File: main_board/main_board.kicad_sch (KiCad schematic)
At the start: 32 parts, among them Q1 NMOS, U1 STM32G031G8Ux, U2 AMS1117-3.3

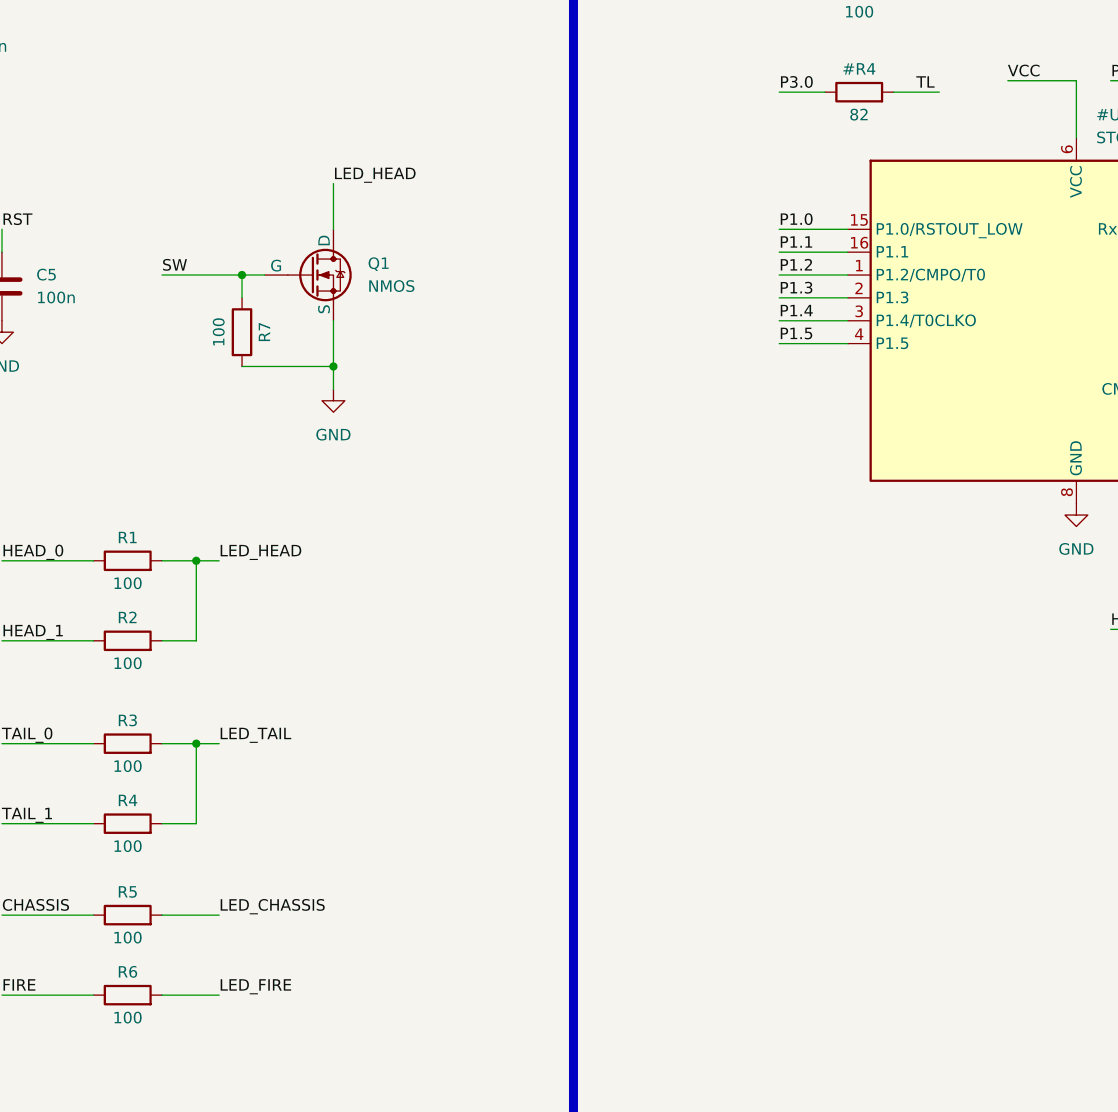
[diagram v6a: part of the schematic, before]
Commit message: feat(main_board): modify placement
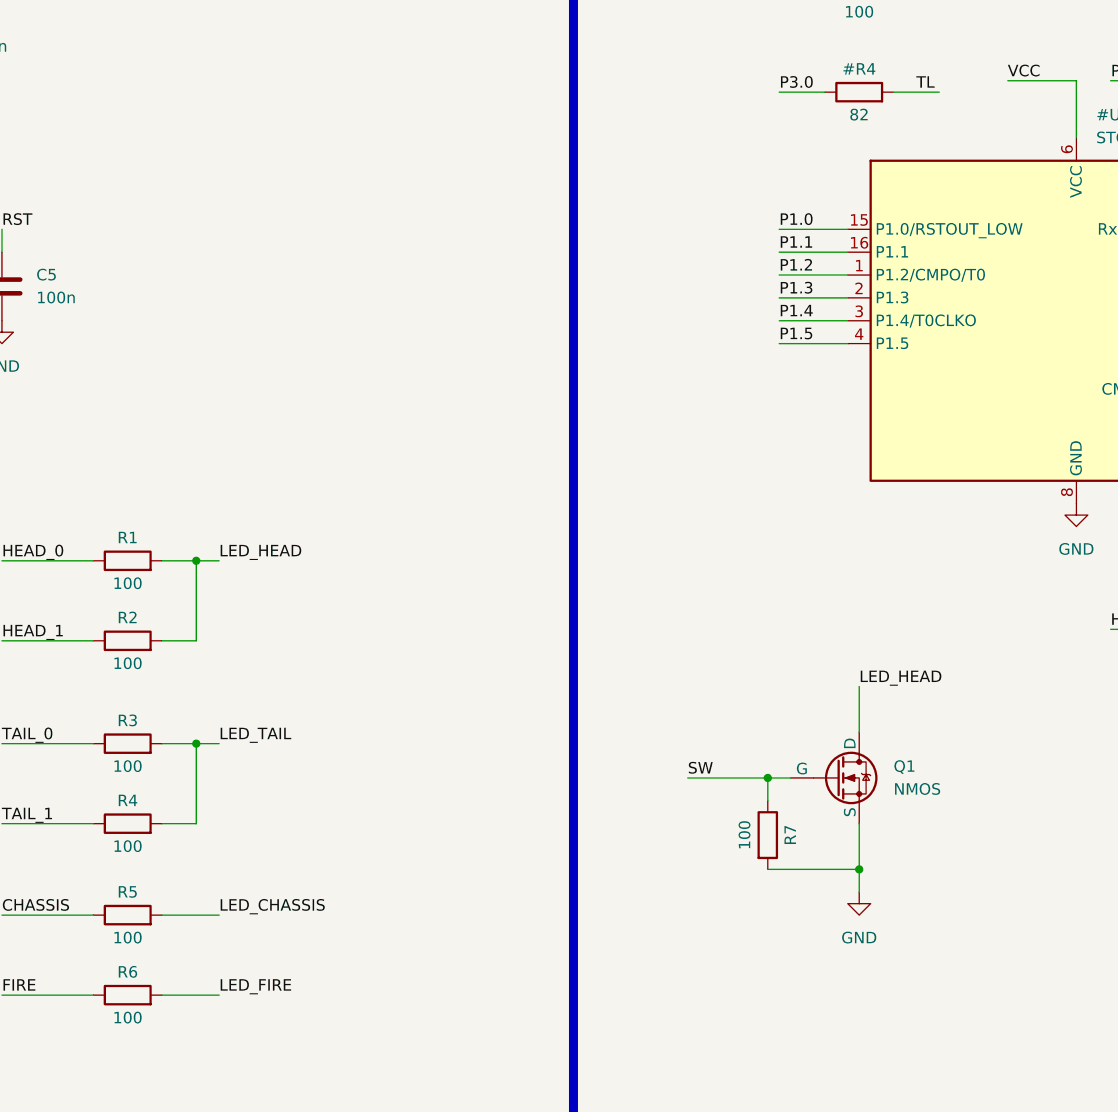
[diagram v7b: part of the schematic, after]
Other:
- moved on the sheet: Q1, R7
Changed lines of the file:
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@@
   (junction (at 119.38 140.97) (diameter 0) (color 0 0 0 0)
   )
-  (junction (at 134.62 99.06) (diameter 0) (color 0 0 0 0)
+  (junction (at 193.04 154.94) (diameter 0) (color 0 0 0 0)
   )
   (junction (at 50.8 58.42) (diameter 0) (color 0 0 0 0)
@@
   (junction (at 119.38 120.65) (diameter 0) (color 0 0 0 0)
   )
-  (junction (at 124.46 88.9) (diameter 0) (color 0 0 0 0)
+  (junction (at 182.88 144.78) (diameter 0) (color 0 0 0 0)
   )
   (no_connect (at 242.57 101.6))
@@
     (stroke (width 0) (type default))
   )
-  (wire (pts (xy 124.46 99.06) (xy 134.62 99.06))
+  (wire (pts (xy 182.88 154.94) (xy 193.04 154.94))
     (stroke (width 0) (type default))
   )
@@
     (stroke (width 0) (type default))
   )
-  (wire (pts (xy 134.62 99.06) (xy 134.62 101.6))
+  (wire (pts (xy 193.04 154.94) (xy 193.04 157.48))
     (stroke (width 0) (type default))
   )
@@
     (stroke (width 0) (type default))
   )
-  (wire (pts (xy 134.62 93.98) (xy 134.62 99.06))
+  (wire (pts (xy 193.04 149.86) (xy 193.04 154.94))
     (stroke (width 0) (type default))
   )
@@
     (stroke (width 0) (type default))
   )
-  (wire (pts (xy 124.46 91.44) (xy 124.46 88.9))
+  (wire (pts (xy 182.88 147.32) (xy 182.88 144.78))
     (stroke (width 0) (type default))
   )
@@
     (stroke (width 0) (type default))
   )
-  (wire (pts (xy 124.46 88.9) (xy 127 88.9))
+  (wire (pts (xy 182.88 144.78) (xy 185.42 144.78))
     (stroke (width 0) (type default))
   )
@@
     (stroke (width 0) (type default))
   )
-  (wire (pts (xy 124.46 88.9) (xy 115.57 88.9))
+  (wire (pts (xy 182.88 144.78) (xy 173.99 144.78))
     (stroke (width 0) (type default))
   )
@@
     (stroke (width 0) (type default))
   )
-  (wire (pts (xy 134.62 78.74) (xy 134.62 83.82))
+  (wire (pts (xy 193.04 134.62) (xy 193.04 139.7))
     (stroke (width 0) (type default))
   )
@@
     (effects (font (size 1.27 1.27)) (justify left bottom))
   )
-  (label "LED_HEAD" (at 134.62 78.74 0) (fields_autoplaced)
+  (label "LED_HEAD" (at 193.04 134.62 0) (fields_autoplaced)
     (effects (font (size 1.27 1.27)) (justify left bottom))
   )
@@
     (effects (font (size 1.27 1.27)) (justify left bottom))
   )
-  (label "SW" (at 115.57 88.9 0) (fields_autoplaced)
+  (label "SW" (at 173.99 144.78 0) (fields_autoplaced)
     (effects (font (size 1.27 1.27)) (justify left bottom))
   )
@@
     )
   )
-  (symbol (lib_id "Device:R") (at 124.46 95.25 0) (unit 1)
+  (symbol (lib_id "Device:R") (at 182.88 151.13 0) (unit 1)
     (in_bom yes) (on_board yes) (dnp no)
-    (property "Reference" "R7" (at 127 95.25 90)
-      (effects (font (size 1.27 1.27)))
-    )
-    (property "Value" "100" (at 121.92 95.25 90)
-      (effects (font (size 1.27 1.27)))
-    )
-    (property "Footprint" "Resistor_SMD:R_0402_1005Metric" (at 122.682 95.25 90)
-      (effects (font (size 1.27 1.27)) hide)
-    )
-    (property "Datasheet" "~" (at 124.46 95.25 0)
-      (effects (font (size 1.27 1.27)) hide)
-    )
-    (property "JLCPCB" "C77623" (at 124.46 95.25 0)
+    (property "Reference" "R7" (at 185.42 151.13 90)
+      (effects (font (size 1.27 1.27)))
+    )
+    (property "Value" "100" (at 180.34 151.13 90)
+      (effects (font (size 1.27 1.27)))
+    )
+    (property "Footprint" "Resistor_SMD:R_0402_1005Metric" (at 181.102 151.13 90)
+      (effects (font (size 1.27 1.27)) hide)
+    )
+    (property "Datasheet" "~" (at 182.88 151.13 0)
+      (effects (font (size 1.27 1.27)) hide)
+    )
+    (property "JLCPCB" "C77623" (at 182.88 151.13 0)
       (effects (font (size 1.27 1.27)) hide)
     )
@@
     )
   )
-  (symbol (lib_id "Simulation_SPICE:NMOS") (at 132.08 88.9 0) (unit 1)
-    (in_bom yes) (on_board yes) (dnp no) (fields_autoplaced)
-    (property "Reference" "Q1" (at 138.43 87.63 0)
-      (effects (font (size 1.27 1.27)) (justify left))
-    )
-    (property "Value" "NMOS" (at 138.43 90.17 0)
-      (effects (font (size 1.27 1.27)) (justify left))
-    )
-    (property "Footprint" "Package_TO_SOT_SMD:SOT-23" (at 137.16 86.36 0)
-      (effects (font (size 1.27 1.27)) hide)
-    )
-    (property "Datasheet" "https://ngspice.sourceforge.io/docs/ngspice-manual.pdf" (at 132.08 101.6 0)
-      (effects (font (size 1.27 1.27)) hide)
-    )
-    (property "Sim.Device" "NMOS" (at 132.08 106.045 0)
-      (effects (font (size 1.27 1.27)) hide)
-    )
-    (property "Sim.Type" "VDMOS" (at 132.08 107.95 0)
-      (effects (font (size 1.27 1.27)) hide)
-    )
-    (property "Sim.Pins" "1=D 2=G 3=S" (at 132.08 104.14 0)
-      (effects (font (size 1.27 1.27)) hide)
-    )
-    (property "JLCPCB" "C22463594" (at 132.08 88.9 0)
+  (symbol (lib_id "Simulation_SPICE:NMOS") (at 190.5 144.78 0) (unit 1)
+    (in_bom yes) (on_board yes) (dnp no) (fields_autoplaced)
+    (property "Reference" "Q1" (at 196.85 143.51 0)
+      (effects (font (size 1.27 1.27)) (justify left))
+    )
+    (property "Value" "NMOS" (at 196.85 146.05 0)
+      (effects (font (size 1.27 1.27)) (justify left))
+    )
+    (property "Footprint" "Package_TO_SOT_SMD:SOT-23" (at 195.58 142.24 0)
+      (effects (font (size 1.27 1.27)) hide)
+    )
+    (property "Datasheet" "https://ngspice.sourceforge.io/docs/ngspice-manual.pdf" (at 190.5 157.48 0)
+      (effects (font (size 1.27 1.27)) hide)
+    )
+    (property "Sim.Device" "NMOS" (at 190.5 161.925 0)
+      (effects (font (size 1.27 1.27)) hide)
+    )
+    (property "Sim.Type" "VDMOS" (at 190.5 163.83 0)
+      (effects (font (size 1.27 1.27)) hide)
+    )
+    (property "Sim.Pins" "1=D 2=G 3=S" (at 190.5 160.02 0)
+      (effects (font (size 1.27 1.27)) hide)
+    )
+    (property "JLCPCB" "C22463594" (at 190.5 144.78 0)
       (effects (font (size 1.27 1.27)) hide)
     )
@@
     )
   )
-  (symbol (lib_id "power:GND") (at 134.62 101.6 0) (unit 1)
-    (in_bom yes) (on_board yes) (dnp no) (fields_autoplaced)
-    (property "Reference" "#PWR016" (at 134.62 107.95 0)
-      (effects (font (size 1.27 1.27)) hide)
-    )
-    (property "Value" "GND" (at 134.62 106.68 0)
-      (effects (font (size 1.27 1.27)))
-    )
-    (property "Footprint" "" (at 134.62 101.6 0)
-      (effects (font (size 1.27 1.27)) hide)
-    )
-    (property "Datasheet" "" (at 134.62 101.6 0)
-      (effects (font (size 1.27 1.27)) hide)
-    )
+  (symbol (lib_id "power:GND") (at 193.04 157.48 0) (unit 1)
+    (in_bom yes) (on_board yes) (dnp no) (fields_autoplaced)
+    (property "Reference" "#PWR016" (at 193.04 163.83 0)
+      (effects (font (size 1.27 1.27)) hide)
+    )
+    (property "Value" "GND" (at 193.04 162.56 0)
+      (effects (font (size 1.27 1.27)))
+    )
+    (property "Footprint" "" (at 193.04 157.48 0)
+      (effects (font (size 1.27 1.27)) hide)
+    )
+    (property "Datasheet" "" (at 193.04 157.48 0)
+      (effects (font (size 1.27 1.27)) hide)
+    )

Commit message: feat(main_board): update jlcpcb part number
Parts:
- C1, C4, C5: JLCPCB C307379 -> C307331
- H2: JLCPCB C5278509 -> C5278509/C510963
- R1, R2, R3, R4, R5, R6, R7: JLCPCB C77623 -> C25076
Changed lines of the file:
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@@
       (effects (font (size 1.27 1.27)) hide)
     )
-    (property "JLCPCB" "C77623" (at 111.76 149.86 0)
+    (property "JLCPCB" "C25076" (at 111.76 149.86 0)
       (effects (font (size 1.27 1.27)) hide)
     )
@@
       (effects (font (size 1.27 1.27)) hide)
     )
-    (property "JLCPCB" "C77623" (at 182.88 151.13 0)
+    (property "JLCPCB" "C25076" (at 182.88 151.13 0)
       (effects (font (size 1.27 1.27)) hide)
     )
@@
       (effects (font (size 1.27 1.27)) hide)
     )
-    (property "JLCPCB" "C5278509" (at 125.73 35.56 0)
+    (property "JLCPCB" "C5278509/C510963" (at 125.73 35.56 0)
       (effects (font (size 1.27 1.27)) hide)
     )
@@
       (effects (font (size 1.27 1.27)) hide)
     )
-    (property "JLCPCB" "C77623" (at 111.76 160.02 0)
+    (property "JLCPCB" "C25076" (at 111.76 160.02 0)
       (effects (font (size 1.27 1.27)) hide)
     )
@@
       (effects (font (size 1.27 1.27)) hide)
     )
-    (property "JLCPCB" "C307379" (at 97.79 90.17 0)
+    (property "JLCPCB" "C307331" (at 97.79 90.17 0)
       (effects (font (size 1.27 1.27)) hide)
     )
@@
       (effects (font (size 1.27 1.27)) hide)
     )
-    (property "JLCPCB" "C307379" (at 90.17 62.23 0)
+    (property "JLCPCB" "C307331" (at 90.17 62.23 0)
       (effects (font (size 1.27 1.27)) hide)
     )
@@
       (effects (font (size 1.27 1.27)) hide)
     )
-    (property "JLCPCB" "C77623" (at 111.76 140.97 0)
+    (property "JLCPCB" "C25076" (at 111.76 140.97 0)
       (effects (font (size 1.27 1.27)) hide)
     )
@@
       (effects (font (size 1.27 1.27)) hide)
     )
-    (property "JLCPCB" "C77623" (at 111.76 120.65 0)
+    (property "JLCPCB" "C25076" (at 111.76 120.65 0)
       (effects (font (size 1.27 1.27)) hide)
     )
@@
       (effects (font (size 1.27 1.27)) hide)
     )
-    (property "JLCPCB" "C307379" (at 38.1 62.23 0)
+    (property "JLCPCB" "C307331" (at 38.1 62.23 0)
       (effects (font (size 1.27 1.27)) hide)
     )
@@
       (effects (font (size 1.27 1.27)) hide)
     )
-    (property "JLCPCB" "C77623" (at 111.76 129.54 0)
+    (property "JLCPCB" "C25076" (at 111.76 129.54 0)
       (effects (font (size 1.27 1.27)) hide)
     )
@@
       (effects (font (size 1.27 1.27)) hide)
     )
-    (property "JLCPCB" "C77623" (at 111.76 168.91 0)
-      (effects (font (size 1.27 1.27)) hide)
-    )
+    (property "JLCPCB" "C25076" (at 111.76 168.91 0)
+      (effects (font (size 1.27 1.27)) hide)
+    )
